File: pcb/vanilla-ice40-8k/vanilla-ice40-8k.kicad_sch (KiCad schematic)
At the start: 12 parts, among them X1 SG-8101CE 100Mhz

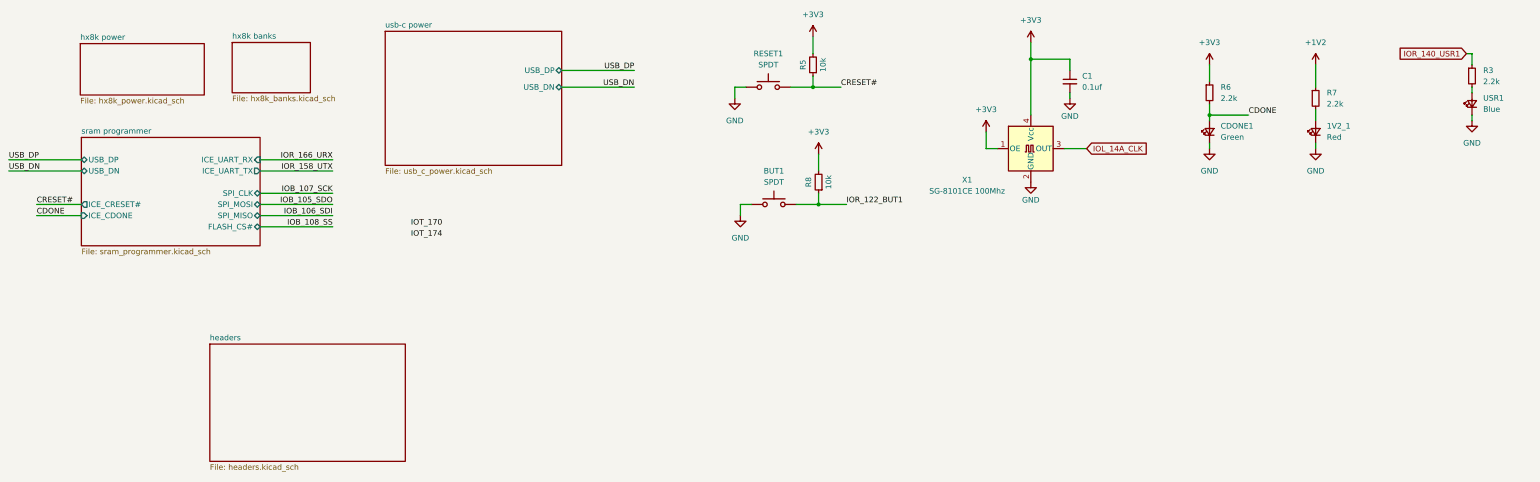
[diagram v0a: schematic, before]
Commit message: [hx8k][pcb] move top level to use symbol lib
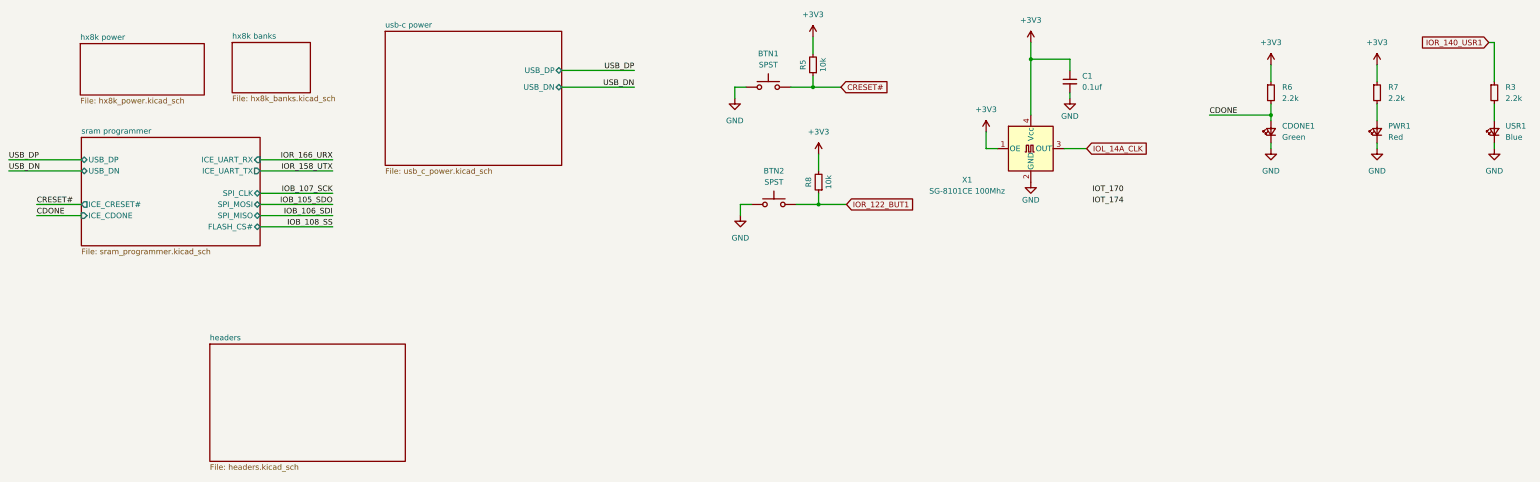
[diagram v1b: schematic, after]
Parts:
- BTN1: renamed from RESET1; value SPDT -> SPST; footprint Button_Switch_SMD:SW_SPST_PTS810 -> !Misc:SW_SPST_PTS810; symbol Switch:SW_Push -> !Misc:BUT_PTS810_BLK
- BTN2: renamed from BUT1; value SPDT -> SPST; footprint Button_Switch_SMD:SW_SPST_PTS810 -> !Misc:SW_SPST_PTS810; symbol Switch:SW_Push -> !Misc:BUT_PTS810_BLK
- C1: symbol Device:C_Small -> !Misc:C_0.1uf_0402
- CDONE1: symbol Device:LED_Small -> !Misc:LED_GRN
- PWR1: renamed from 1V2_1; symbol Device:LED_Small -> !Misc:LED_RED
- R3, R6, R7: symbol Device:R_Small -> !Misc:R_2.2K_0603
- R5, R8: symbol Device:R_Small -> !Misc:R_10K_0603
- USR1: symbol Device:LED_Small -> !Misc:LED_BLU
- X1: symbol Oscillator:SG-8002CE -> !Misc:SG-8101CE
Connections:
- net +1V2 is gone; now on net +3V3: R7.1
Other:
- moved on the sheet: CDONE1, PWR1, R3, R6, R7, USR1

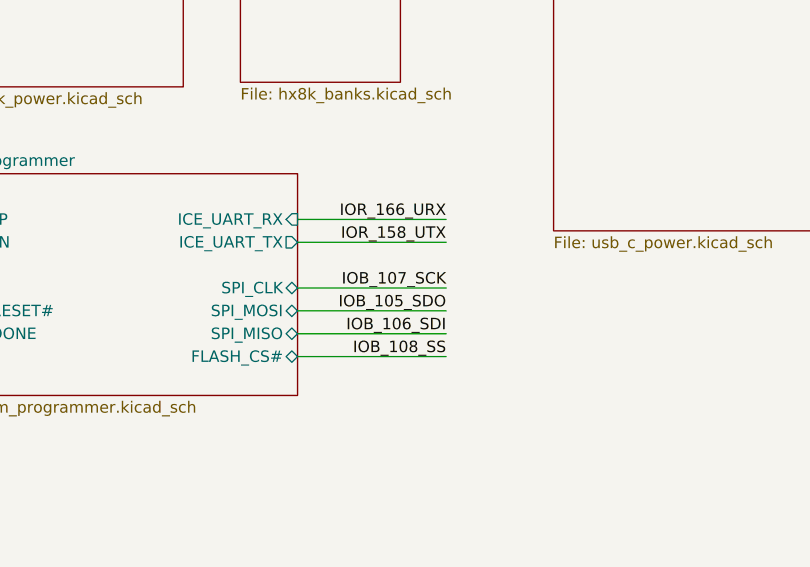
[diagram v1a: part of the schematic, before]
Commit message: [hx8k][pcb] move programmer to symbol lib
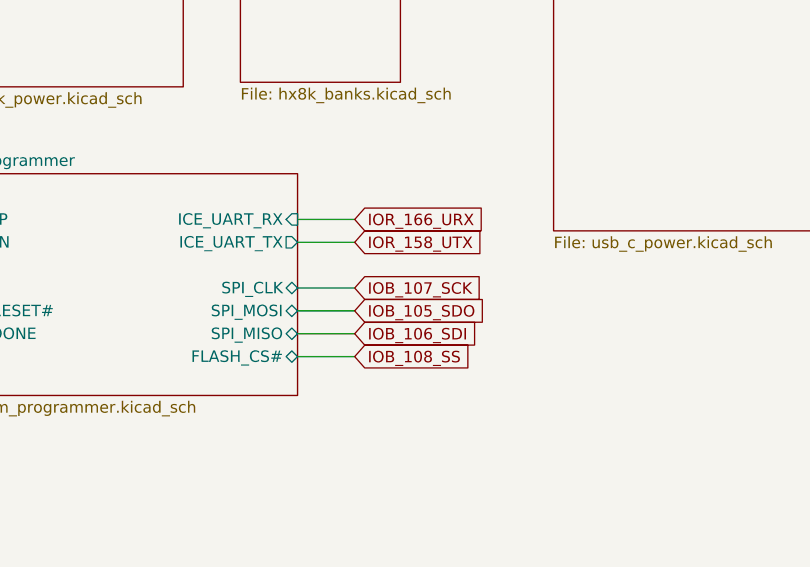
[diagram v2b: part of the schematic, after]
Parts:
- BTN1, BTN2: Digi-Key Part Number CKN10503CT-ND -> CKN10878CT-ND
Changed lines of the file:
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@@
 	(wire
 		(pts
-			(xy 69.85 64.77) (xy 86.36 64.77)
+			(xy 69.85 64.77) (xy 76.2 64.77)
 		)
 		(stroke
@@
 	(wire
 		(pts
-			(xy 69.85 59.69) (xy 86.36 59.69)
+			(xy 69.85 59.69) (xy 76.2 59.69)
 		)
 		(stroke
@@
 	(wire
 		(pts
-			(xy 69.85 62.23) (xy 86.36 62.23)
+			(xy 69.85 62.23) (xy 76.2 62.23)
 		)
 		(stroke
@@
 	(wire
 		(pts
-			(xy 69.85 52.07) (xy 86.36 52.07)
+			(xy 69.85 52.07) (xy 76.2 52.07)
 		)
 		(stroke
@@
 	(wire
 		(pts
-			(xy 69.85 49.53) (xy 86.36 49.53)
+			(xy 69.85 49.53) (xy 76.2 49.53)
 		)
 		(stroke
@@
 	(wire
 		(pts
-			(xy 69.85 57.15) (xy 86.36 57.15)
+			(xy 69.85 57.15) (xy 76.2 57.15)
 		)
 		(stroke
@@
 		)
 	)
-	(label "IOR_158_UTX"
-		(at 86.36 52.07 180)
-		(effects
-			(font
-				(size 1.27 1.27)
-			)
-			(justify right bottom)
-		)
-	)
 	(label "CDONE"
 		(at 19.05 62.23 0)
@@
 		)
 	)
-	(label "IOB_106_SDI"
-		(at 86.36 62.23 180)
-		(effects
-			(font
-				(size 1.27 1.27)
-			)
-			(justify right bottom)
-		)
-	)
 	(label "USB_DN"
 		(at 12.7 52.07 0)
@@
 		)
 	)
-	(label "IOR_166_URX"
-		(at 86.36 49.53 180)
-		(effects
-			(font
-				(size 1.27 1.27)
-			)
-			(justify right bottom)
-		)
-	)
-	(label "IOB_108_SS"
-		(at 86.36 64.77 180)
-		(effects
-			(font
-				(size 1.27 1.27)
-			)
-			(justify right bottom)
-		)
-	)
 	(label "CDONE"
 		(at 285.75 39.37 0)
@@
 		)
 	)
-	(label "IOB_105_SDO"
-		(at 86.36 59.69 180)
-		(effects
-			(font
-				(size 1.27 1.27)
-			)
-			(justify right bottom)
-		)
-	)
-	(label "IOB_107_SCK"
-		(at 86.36 57.15 180)
-		(effects
-			(font
-				(size 1.27 1.27)
-			)
-			(justify right bottom)
-		)
-	)
 	(label "IOT_170"
 		(at 259.08 57.15 0)
@@
 		)
 	)
+	(global_label "IOR_166_URX"
+		(shape input)
+		(at 76.2 49.53 0)
+		(fields_autoplaced yes)
+		(effects
+			(font
+				(size 1.27 1.27)
+			)
+			(justify left)
+		)
+		(property "Intersheetrefs" "${INTERSHEET_REFS}"
+			(at 91.7642 49.53 0)
+			(effects
+				(font
+					(size 1.27 1.27)
+				)
+				(justify left)
+				(hide yes)
+			)
+		)
+	)
 	(global_label "CRESET#"
 		(shape input)
@@
 		)
 	)
+	(global_label "IOB_107_SCK"
+		(shape input)
+		(at 76.2 57.15 0)
+		(fields_autoplaced yes)
+		(effects
+			(font
+				(size 1.27 1.27)
+			)
+			(justify left)
+		)
+		(property "Intersheetrefs" "${INTERSHEET_REFS}"
+			(at 91.7037 57.15 0)
+			(effects
+				(font
+					(size 1.27 1.27)
+				)
+				(justify left)
+				(hide yes)
+			)
+		)
+	)
+	(global_label "IOB_105_SDO"
+		(shape input)
+		(at 76.2 59.69 0)
+		(fields_autoplaced yes)
+		(effects
+			(font
+				(size 1.27 1.27)
+			)
+			(justify left)
+		)
+		(property "Intersheetrefs" "${INTERSHEET_REFS}"
+			(at 91.7642 59.69 0)
+			(effects
+				(font
+					(size 1.27 1.27)
+				)
+				(justify left)
+				(hide yes)
+			)
+		)
+	)
 	(global_label "IOL_14A_CLK"
 		(shape input)
@@
 		)
 	)
+	(global_label "IOR_158_UTX"
+		(shape input)
+		(at 76.2 52.07 0)
+		(fields_autoplaced yes)
+		(effects
+			(font
+				(size 1.27 1.27)
+			)
+			(justify left)
+		)
+		(property "Intersheetrefs" "${INTERSHEET_REFS}"
+			(at 91.4618 52.07 0)
+			(effects
+				(font
+					(size 1.27 1.27)
+				)
+				(justify left)
+				(hide yes)
+			)
+		)
+	)
 	(global_label "IOR_140_USR1"
 		(shape input)
@@
 				)
 				(justify right)
+				(hide yes)
+			)
+		)
+	)
+	(global_label "IOB_108_SS"
+		(shape input)
+		(at 76.2 64.77 0)
+		(fields_autoplaced yes)
+		(effects
+			(font
+				(size 1.27 1.27)
+			)
+			(justify left)
+		)
+		(property "Intersheetrefs" "${INTERSHEET_REFS}"
+			(at 90.3732 64.77 0)
+			(effects
+				(font
+					(size 1.27 1.27)
+				)
+				(justify left)
+				(hide yes)
+			)
+		)
+	)
+	(global_label "IOB_106_SDI"
+		(shape input)
+		(at 76.2 62.23 0)
+		(fields_autoplaced yes)
+		(effects
+			(font
+				(size 1.27 1.27)
+			)
+			(justify left)
+		)
+		(property "Intersheetrefs" "${INTERSHEET_REFS}"
+			(at 91.0385 62.23 0)
+			(effects
+				(font
+					(size 1.27 1.27)
+				)
+				(justify left)
 				(hide yes)
 			)
@@
 			)
 		)
-		(property "Description" "Push button switch, generic, two pins"
+		(property "Description" "PTS810 SPST Black, 600 grams"
 			(at 186.69 59.69 0)
 			(effects
@@
 			)
 		)
-		(property "Digi-Key Part Number" "CKN10503CT-ND"
+		(property "Digi-Key Part Number" "CKN10878CT-ND"
 			(at 186.69 59.69 0)
 			(effects
@@
 			)
 		)
-		(property "Description" "Push button switch, generic, two pins"
+		(property "Description" "PTS810 SPST Black, 600 grams"
 			(at 185.42 33.02 0)
 			(effects
@@
 			)
 		)
-		(property "Digi-Key Part Number" "CKN10503CT-ND"
+		(property "Digi-Key Part Number" "CKN10878CT-ND"
 			(at 185.42 33.02 0)
 			(effects

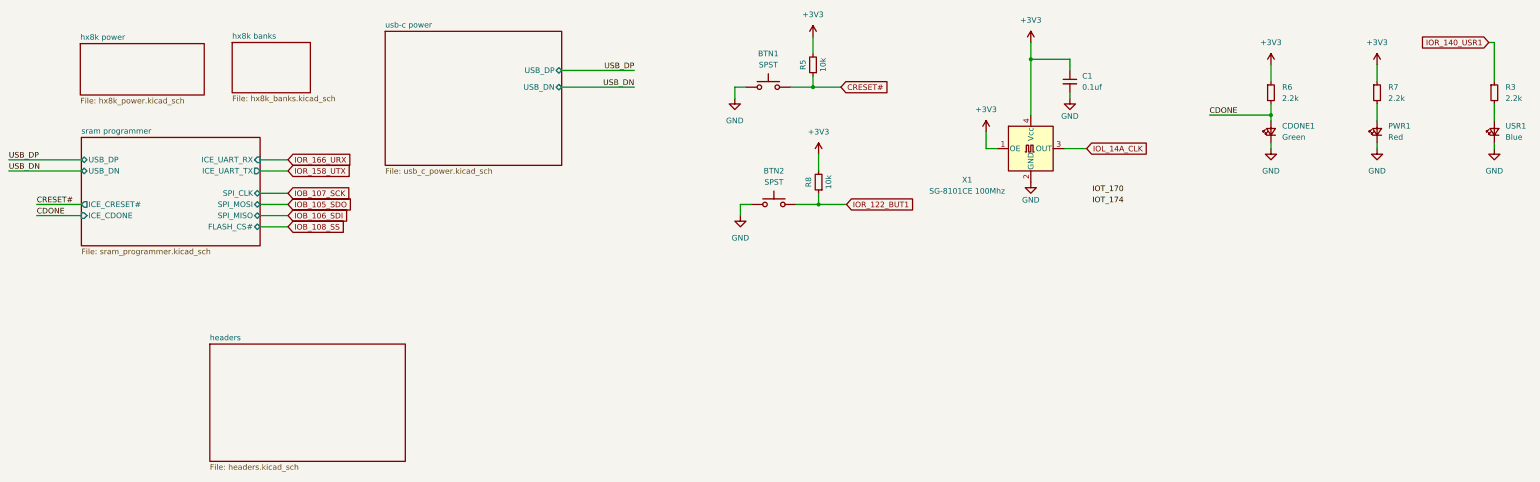
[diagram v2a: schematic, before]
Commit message: [hx8k][pcb] completed all moves to lib other than ice40
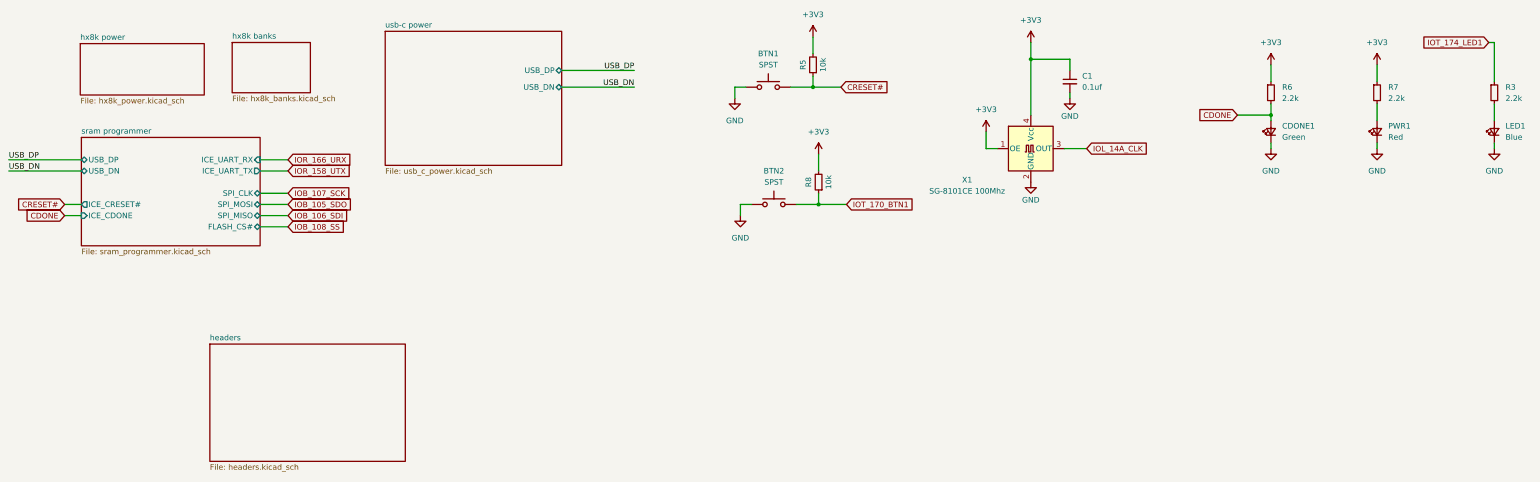
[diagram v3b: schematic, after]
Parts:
- renumbered USR1 to LED1
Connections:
- net IOR_122_BUT1 renamed IOT_170_BTN1
- net IOR_140_USR1 renamed IOT_174_LED1
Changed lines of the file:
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@@
 	(wire
 		(pts
-			(xy 19.05 59.69) (xy 29.21 59.69)
+			(xy 25.4 59.69) (xy 29.21 59.69)
 		)
 		(stroke
@@
 	(wire
 		(pts
-			(xy 19.05 62.23) (xy 29.21 62.23)
+			(xy 25.4 62.23) (xy 29.21 62.23)
 		)
 		(stroke
@@
 	(wire
 		(pts
-			(xy 299.72 39.37) (xy 285.75 39.37)
+			(xy 299.72 39.37) (xy 292.1 39.37)
 		)
 		(stroke
@@
 		)
 	)
-	(label "CDONE"
-		(at 19.05 62.23 0)
-		(effects
-			(font
-				(size 1.27 1.27)
-			)
-			(justify left bottom)
-		)
-	)
 	(label "USB_DN"
 		(at 12.7 52.07 0)
@@
 		)
 	)
-	(label "IOT_174"
-		(at 259.08 59.69 0)
-		(effects
-			(font
-				(size 1.27 1.27)
-			)
-			(justify left bottom)
-		)
-	)
-	(label "CDONE"
-		(at 285.75 39.37 0)
-		(effects
-			(font
-				(size 1.27 1.27)
-			)
-			(justify left bottom)
-		)
-	)
-	(label "IOT_170"
-		(at 259.08 57.15 0)
-		(effects
-			(font
-				(size 1.27 1.27)
-			)
-			(justify left bottom)
-		)
-	)
 	(label "USB_DP"
 		(at 154.94 29.21 180)
@@
 		)
 	)
-	(label "CRESET#"
-		(at 19.05 59.69 0)
-		(effects
-			(font
-				(size 1.27 1.27)
-			)
-			(justify left bottom)
+	(global_label "CDONE"
+		(shape input)
+		(at 292.1 39.37 180)
+		(fields_autoplaced yes)
+		(effects
+			(font
+				(size 1.27 1.27)
+			)
+			(justify right)
+		)
+		(property "Intersheetrefs" "${INTERSHEET_REFS}"
+			(at 282.7648 39.37 0)
+			(effects
+				(font
+					(size 1.27 1.27)
+				)
+				(justify right)
+				(hide yes)
+			)
 		)
 	)
@@
 		)
 	)
+	(global_label "CRESET#"
+		(shape input)
+		(at 25.4 59.69 180)
+		(fields_autoplaced yes)
+		(effects
+			(font
+				(size 1.27 1.27)
+			)
+			(justify right)
+		)
+		(property "Intersheetrefs" "${INTERSHEET_REFS}"
+			(at 14.1297 59.69 0)
+			(effects
+				(font
+					(size 1.27 1.27)
+				)
+				(justify right)
+				(hide yes)
+			)
+		)
+	)
 	(global_label "IOB_107_SCK"
 		(shape input)
@@
 		)
 	)
+	(global_label "CDONE"
+		(shape input)
+		(at 25.4 62.23 180)
+		(fields_autoplaced yes)
+		(effects
+			(font
+				(size 1.27 1.27)
+			)
+			(justify right)
+		)
+		(property "Intersheetrefs" "${INTERSHEET_REFS}"
+			(at 16.0648 62.23 0)
+			(effects
+				(font
+					(size 1.27 1.27)
+				)
+				(justify right)
+				(hide yes)
+			)
+		)
+	)
 	(global_label "IOR_158_UTX"
 		(shape input)
@@
 		)
 	)
-	(global_label "IOR_140_USR1"
+	(global_label "IOT_174_LED1"
 		(shape input)
 		(at 349.25 22.86 180)
@@
 		)
 		(property "Intersheetrefs" "${INTERSHEET_REFS}"
-			(at 332.4763 22.86 0)
+			(at 333.1416 22.86 0)
 			(effects
 				(font
@@
 		)
 	)
-	(global_label "IOR_122_BUT1"
+	(global_label "IOT_170_BTN1"
 		(shape input)
 		(at 203.2 59.69 0)
@@
 		)
 		(property "Intersheetrefs" "${INTERSHEET_REFS}"
-			(at 219.7318 59.69 0)
+			(at 219.4294 59.69 0)
 			(effects
 				(font
@@
 		(dnp no)
 		(fields_autoplaced yes)
-		(property "Reference" "USR1"
+		(property "Reference" "LED1"
 			(at 353.06 41.8464 90)
 			(effects
@@
 			(project "vanilla-ice40-8k"
 				(path "/6fdfbf4b-014a-4077-8dc3-7ce5ecaf5fe5"
-					(reference "USR1")
+					(reference "LED1")
 					(unit 1)
 				)

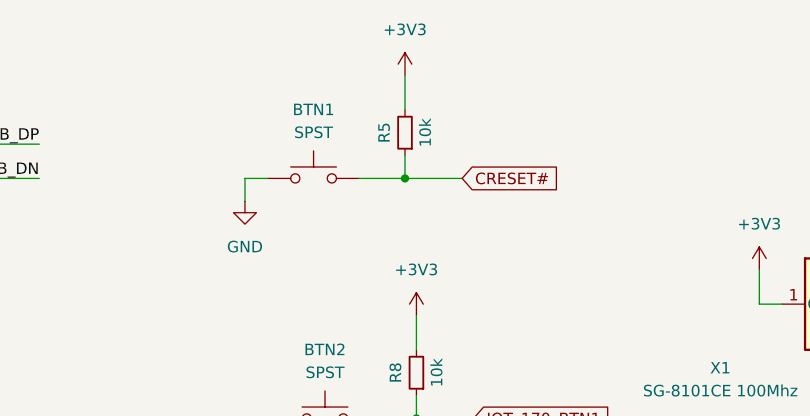
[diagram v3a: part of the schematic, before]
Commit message: [hx8k][pcb] start of routing programmer
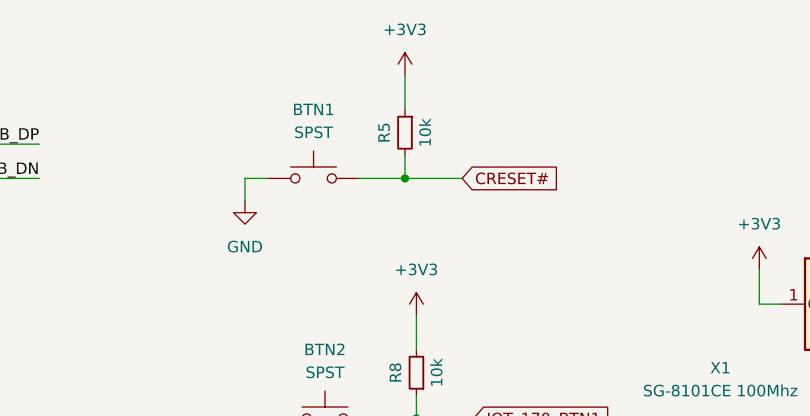
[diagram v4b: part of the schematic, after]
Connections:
- net +3V3: now also R5.1; no longer R5.2
- net CRESET#: now also R5.2; no longer R5.1
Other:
- moved on the sheet: R5
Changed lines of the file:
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@@
 	(symbol
 		(lib_id "!Misc:R_10K_0603")
-		(at 195.58 27.94 180)
+		(at 195.58 27.94 0)
+		(mirror y)
 		(unit 1)
 		(exclude_from_sim no)

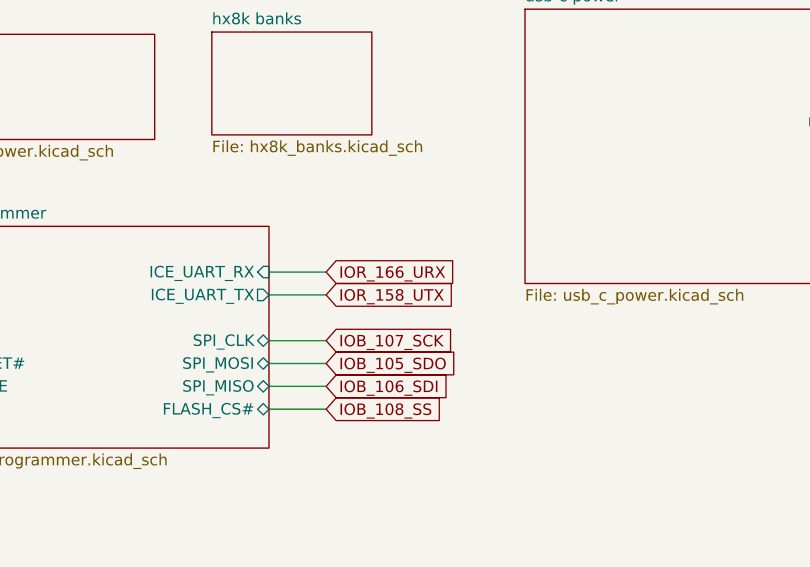
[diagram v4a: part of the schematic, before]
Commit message: [hx8k][pcb] ft routed
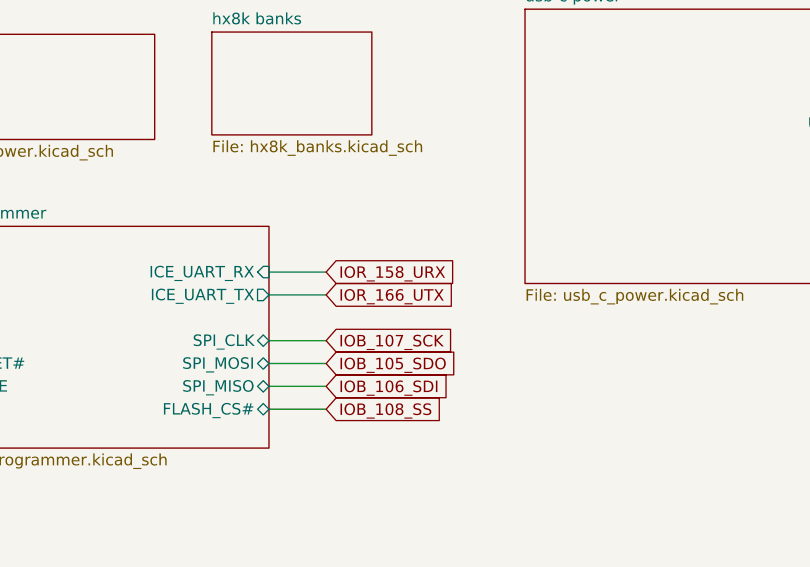
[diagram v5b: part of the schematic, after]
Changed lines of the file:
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@@
 		)
 	)
-	(global_label "IOR_166_URX"
+	(global_label "IOR_166_UTX"
 		(shape input)
-		(at 76.2 49.53 0)
+		(at 76.2 52.07 0)
 		(fields_autoplaced yes)
 		(effects
@@
 		)
 		(property "Intersheetrefs" "${INTERSHEET_REFS}"
-			(at 91.7642 49.53 0)
+			(at 91.4618 52.07 0)
 			(effects
 				(font
@@
 		)
 	)
-	(global_label "IOR_158_UTX"
+	(global_label "IOR_158_URX"
 		(shape input)
-		(at 76.2 52.07 0)
+		(at 76.2 49.53 0)
 		(fields_autoplaced yes)
 		(effects
@@
 		)
 		(property "Intersheetrefs" "${INTERSHEET_REFS}"
-			(at 91.4618 52.07 0)
+			(at 91.7642 49.53 0)
 			(effects
 				(font
